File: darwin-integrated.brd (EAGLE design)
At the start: 96 x 62 mm, 44 parts

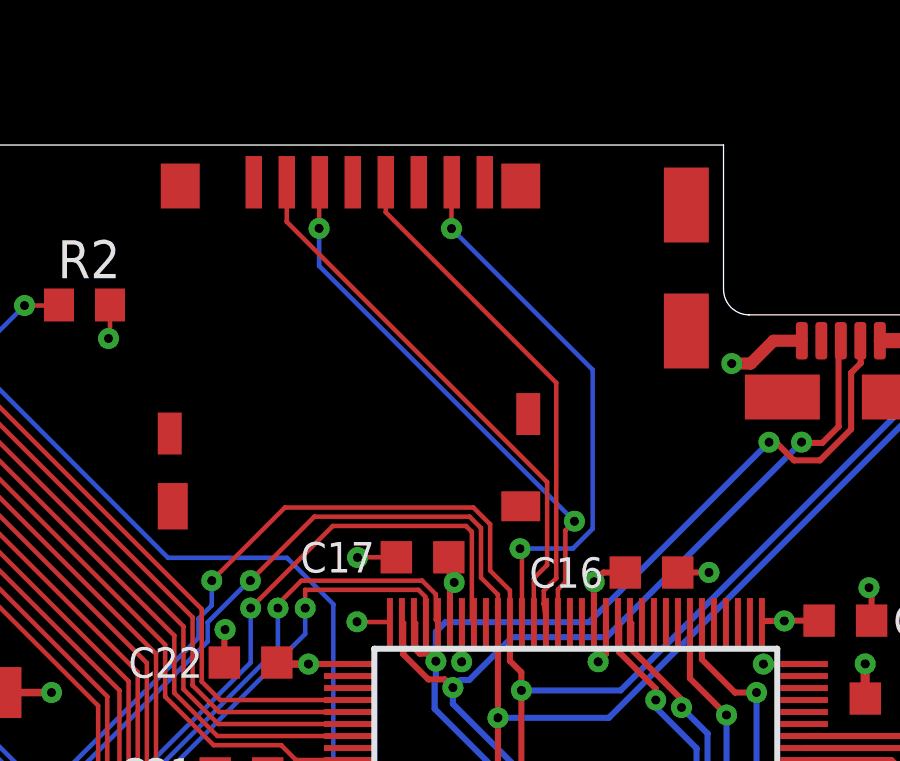
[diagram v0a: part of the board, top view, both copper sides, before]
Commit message: Fixed SD Power Disconnect.
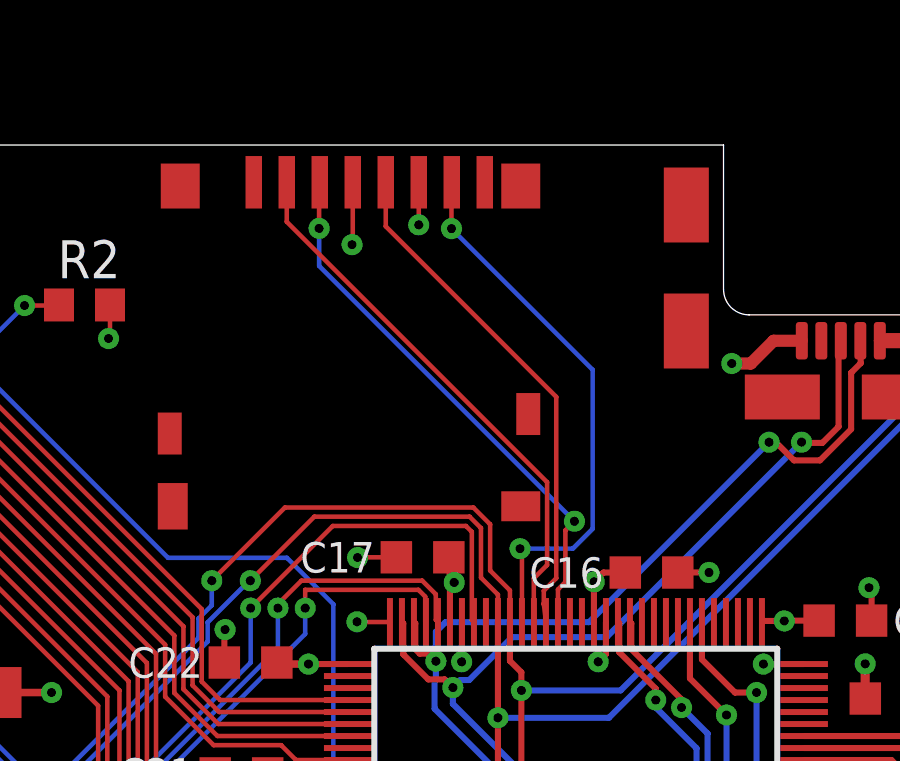
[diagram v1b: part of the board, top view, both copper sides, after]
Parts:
- LOWER, UPPER: value MOLEX-15-91-2200 -> MOLEX-15-91-2200F; device Conservify:20PH -> Conservify:20PH-F
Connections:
- net 3V3: now also U$9.VDD
- net GND: now also U$9.VSS
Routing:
- net 3V3: track 68.0 -> 70.1 mm, vias 28 -> 29
- net GND: track 98.6 -> 100.1 mm, vias 43 -> 44

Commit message: Panelized. PA1.
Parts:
- added FID1, FID2, FID3, FID4, FID5, FID6: FIDUCIAL_1MM, microbuilder:FIDUCIAL_1MM
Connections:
- net MOD_G1 renamed EEPROM_PROT
- net MOD_G3 renamed HOTSWAP_INT
- removed net N$1: D1.C, RTC.3, U$7.+
- removed net UPPER_PIN10: UPPER.PIN10
- new net VBACKUP: D1.C, RTC.3, U$7.+, UPPER.PIN10
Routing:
- net VBACKUP: track 0.00 -> 66.6 mm, vias 0 -> 2
- net N$1: track 22.5 -> 0.00 mm
- net CORE_SDA: track 114.7 -> 108.1 mm
- net CORE_SCL: track 112.9 -> 106.6 mm
- net RESET: track 62.2 -> 61.3 mm
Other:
- outline, holes or cut-outs redrawn

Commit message: Cleanup.
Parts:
- C1, C10, C11, C12, C13, C14, C15, C16, C17, C18, C19, C2, C20, C3, C4, C5, C8, C9: value (none) -> .1uf
- C23: value DSK-3R3H204T614-H2L -> .2f
- C6: value .1u -> .1uf
- C7: value 4.7u -> 4.7uf
- D1: value (none) -> VS-10BQ015HM3/5BT
- R1: value (none) -> 2k
- R2: value (none) -> 10k
- R3, R4: value (none) -> 4.7k
- R5: value (none) -> 10K
- renumbered C21 to C9, C22 to C8, U$10 to SCREEN, U$3 to U1, U$4 to U2, U$5 to U3, U$6 to U4, U$7 to C23, U$8 to USB, U$9 to SD
